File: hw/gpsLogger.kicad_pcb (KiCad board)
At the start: 4 copper layers, 41 x 72.8 mm, 210 parts, among them IC1 MSP430F55xx, P1 USB_OTG, Q2 FG6943010R, SW1 SW_PUSH, U1 MAX_M8Q, U2 MCP73812, U3 uSD, U4 MIC2091, U5 MIC2091, U6 TPS78230, X1 CRYSTAL_SMD

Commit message: Finished routing
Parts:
- removed the REF** at (150.2, 122.0)
- removed the REF** at (152.2, 122.0)
- removed the REF** at (156.2, 122.0)
- removed the REF** at (150.2, 118.0)
- removed the REF** at (150.2, 120.0)
- removed the REF** at (156.2, 120.0)
- removed the REF** at (152.2, 120.0)
- removed the REF** at (164.2, 107.6)
- removed the REF** at (150.0, 97.2)
- removed the REF** at (170.2, 108.0)
- removed the REF** at (170.2, 110.0)
- removed the REF** at (165.2, 120.0)
- removed the REF** at (170.2, 122.0)
- removed the REF** at (168.2, 122.0)
- removed the REF** at (168.2, 124.0)
- removed the REF** at (168.2, 126.0)
- removed the REF** at (164.2, 128.0)
- removed the REF** at (164.2, 130.0)
- added P2: CONN_01X02, footprints:BM02B-GHS-TBT, F.Cu at (166.4, 132.2)
- added REF**: SolderWirePad_single_0-8mmDrill, Wire_Pads:SolderWirePad_single_0-8mmDrill, F.Cu at (153.2, 115.4)
- added REF**: SolderWirePad_single_0-8mmDrill, Wire_Pads:SolderWirePad_single_0-8mmDrill, F.Cu at (169.0, 115.0)
- added REF**: SolderWirePad_single_0-8mmDrill, Wire_Pads:SolderWirePad_single_0-8mmDrill, F.Cu at (158.2, 68.0)
- added REF**: SolderWirePad_single_0-8mmDrill, Wire_Pads:SolderWirePad_single_0-8mmDrill, F.Cu at (168.8, 80.6)
- added REF**: SolderWirePad_single_0-8mmDrill, Wire_Pads:SolderWirePad_single_0-8mmDrill, F.Cu at (164.4, 99.6)
- added REF**: SolderWirePad_single_0-8mmDrill, Wire_Pads:SolderWirePad_single_0-8mmDrill, F.Cu at (162.0, 108.0)
- added REF**: SolderWirePad_single_0-8mmDrill, Wire_Pads:SolderWirePad_single_0-8mmDrill, F.Cu at (156.0, 108.0)
- added REF**: SolderWirePad_single_0-8mmDrill, Wire_Pads:SolderWirePad_single_0-8mmDrill, F.Cu at (154.0, 108.0)
- added REF**: SolderWirePad_single_0-8mmDrill, Wire_Pads:SolderWirePad_single_0-8mmDrill, F.Cu at (152.0, 108.0)
- added REF**: SolderWirePad_single_0-8mmDrill, Wire_Pads:SolderWirePad_single_0-8mmDrill, F.Cu at (168.4, 106.8)
- added REF**: SolderWirePad_single_0-8mmDrill, Wire_Pads:SolderWirePad_single_0-8mmDrill, F.Cu at (164.0, 124.0)
- added REF**: SolderWirePad_single_0-8mmDrill, Wire_Pads:SolderWirePad_single_0-8mmDrill, F.Cu at (153.4, 124.0)
- added REF**: SolderWirePad_single_0-8mmDrill, Wire_Pads:SolderWirePad_single_0-8mmDrill, F.Cu at (164.0, 122.0)
- added REF**: SolderWirePad_single_0-8mmDrill, Wire_Pads:SolderWirePad_single_0-8mmDrill, F.Cu at (164.0, 120.0)
- added REF**: SolderWirePad_single_0-8mmDrill, Wire_Pads:SolderWirePad_single_0-8mmDrill, F.Cu at (164.0, 118.0)
- added REF**: SolderWirePad_single_0-8mmDrill, Wire_Pads:SolderWirePad_single_0-8mmDrill, F.Cu at (164.0, 116.0)
- added REF**: SolderWirePad_single_0-8mmDrill, Wire_Pads:SolderWirePad_single_0-8mmDrill, F.Cu at (162.0, 116.0)
- added REF**: SolderWirePad_single_0-8mmDrill, Wire_Pads:SolderWirePad_single_0-8mmDrill, F.Cu at (162.0, 118.0)
- added REF**: SolderWirePad_single_0-8mmDrill, Wire_Pads:SolderWirePad_single_0-8mmDrill, F.Cu at (160.0, 118.0)
- added REF**: SolderWirePad_single_0-8mmDrill, Wire_Pads:SolderWirePad_single_0-8mmDrill, F.Cu at (158.0, 118.0)
- added REF**: SolderWirePad_single_0-8mmDrill, Wire_Pads:SolderWirePad_single_0-8mmDrill, F.Cu at (158.0, 122.0)
- added REF**: SolderWirePad_single_0-8mmDrill, Wire_Pads:SolderWirePad_single_0-8mmDrill, F.Cu at (158.0, 124.0)
- added REF**: SolderWirePad_single_0-8mmDrill, Wire_Pads:SolderWirePad_single_0-8mmDrill, F.Cu at (151.2, 120.4)
- added REF**: SolderWirePad_single_0-8mmDrill, Wire_Pads:SolderWirePad_single_0-8mmDrill, F.Cu at (160.0, 124.0)
- added REF**: SolderWirePad_single_0-8mmDrill, Wire_Pads:SolderWirePad_single_0-8mmDrill, F.Cu at (160.0, 122.0)
- added REF**: SolderWirePad_single_0-8mmDrill, Wire_Pads:SolderWirePad_single_0-8mmDrill, F.Cu at (150.0, 123.0)
- added REF**: SolderWirePad_single_0-8mmDrill, Wire_Pads:SolderWirePad_single_0-8mmDrill, F.Cu at (171.8, 110.0)
- added REF**: SolderWirePad_single_0-8mmDrill, Wire_Pads:SolderWirePad_single_0-8mmDrill, F.Cu at (171.2, 118.0)
- added REF**: SolderWirePad_single_0-8mmDrill, Wire_Pads:SolderWirePad_single_0-8mmDrill, F.Cu at (170.8, 120.0)
- added REF**: SolderWirePad_single_0-8mmDrill, Wire_Pads:SolderWirePad_single_0-8mmDrill, F.Cu at (170.6, 122.0)
- added REF**: SolderWirePad_single_0-8mmDrill, Wire_Pads:SolderWirePad_single_0-8mmDrill, F.Cu at (170.6, 124.0)
- ANT1, U1: moved to B.Cu
- FB1: footprint Resistors_SMD:R_0805 -> Resistors_SMD:R_0603
- moved REF** 13.1 mm to (148.0, 86.0)
- moved ANT1 11.4 mm to (149.8, 117.0), turned to 180 degrees
- moved REF** 8.85 mm to (148.0, 90.0)
- moved C5 8.63 mm to (153.3, 117.5), turned to 90 degrees
- moved U4 8.36 mm to (168.4, 109.4), turned to 270 degrees
- moved U1 8.07 mm to (160.8, 120.0), turned to 0 degrees
- moved R5 7.56 mm to (168.2, 116.8), turned to 90 degrees
- moved L2 7.52 mm to (165.8, 112.6), turned to 270 degrees
- moved R6 6.42 mm to (153.3, 120.0)
- moved R8 6.00 mm to (169.8, 116.8), turned to 270 degrees
- moved REF** 5.75 mm to (151.3, 119.0)
- moved L1 4.88 mm to (151.8, 121.5)
- moved R9 4.80 mm to (168.4, 112.4), turned to 180 degrees
- moved C13 4.53 mm to (168.4, 126.0), turned to 270 degrees
- moved REF** 3.94 mm to (148.0, 98.0)
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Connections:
- IC1 pad 19: Net-(IC1-Pad19) -> ~CHG
- IC1 pad 52: Net-(IC1-Pad52) -> /DM
- IC1 pad 65: GND -> (no net)
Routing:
- net ~CHG: track 0.00 -> 60.8 mm, vias 0 -> 4
- net GPS_BACKUP: track 23.5 -> 42.8 mm, vias 1 -> 2
- net GPS_PPS: track 24.8 -> 41.3 mm, vias 1 -> 2
- net GPS_MOSI: track 28.0 -> 41.5 mm, vias 1 -> 2
- net GPS_MISO: track 28.7 -> 40.6 mm, vias 1 -> 2
- net Net-(R5-Pad1): track 6.08 -> 14.3 mm, vias 1 -> 2
- net Net-(R8-Pad2): track 15.3 -> 9.36 mm
- net +3V3: track 25.3 -> 20.1 mm
- net GPS_VCC_RF: track 6.82 -> 2.00 mm, vias 1 -> 0
- net +BATT: track 23.1 -> 25.9 mm, vias 0 -> 1
- net GPS_VCC: track 56.9 -> 54.4 mm, vias 4 -> 3
- net GND: track 29.7 -> 31.7 mm, vias 3 -> 1
- net GPS_PWR_FAULT: track 36.1 -> 34.3 mm
- net Net-(IC1-Pad52): track 1.33 -> 0.00 mm
- net /DM: track 7.12 -> 8.45 mm
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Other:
- outline, holes or cut-outs redrawn
- board text removed: "github.com/Greeeg/gpsLogger"

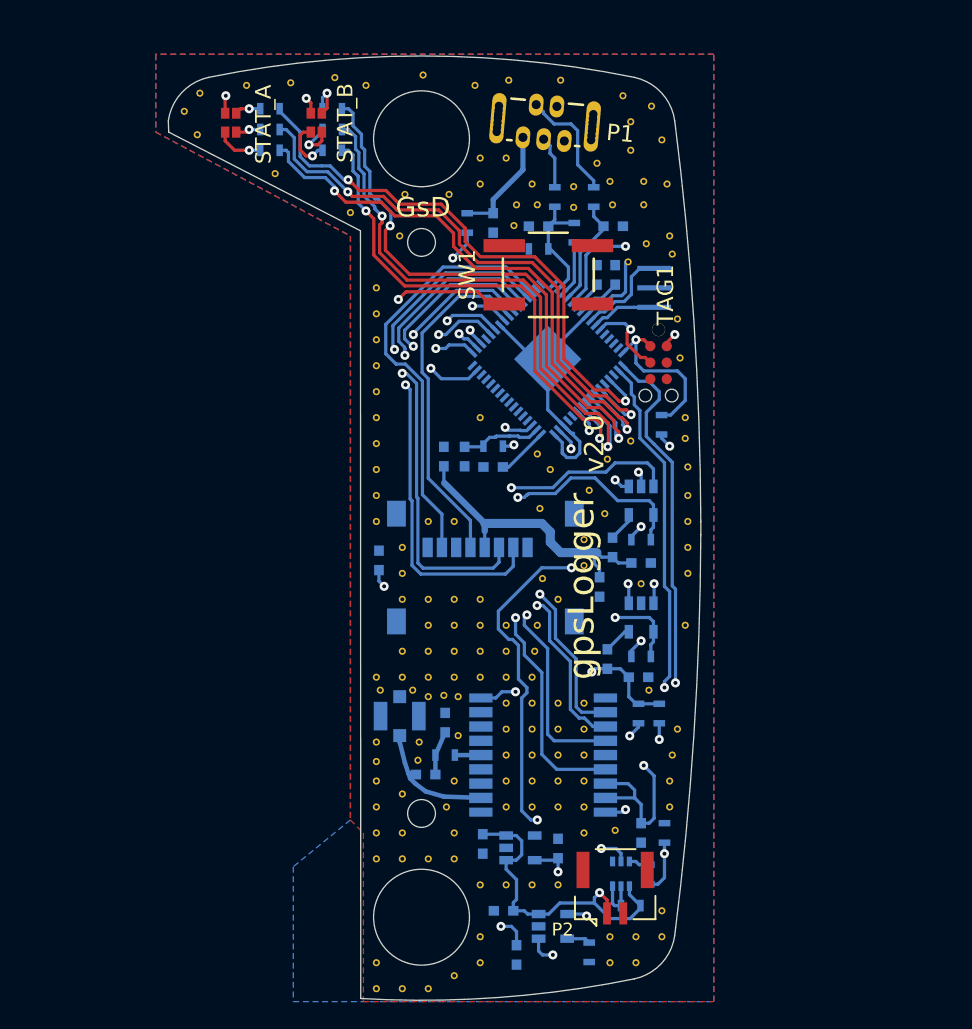
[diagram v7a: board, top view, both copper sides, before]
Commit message: Added PCB mount antenna and LNA + SAW filter. Re-routed PCB
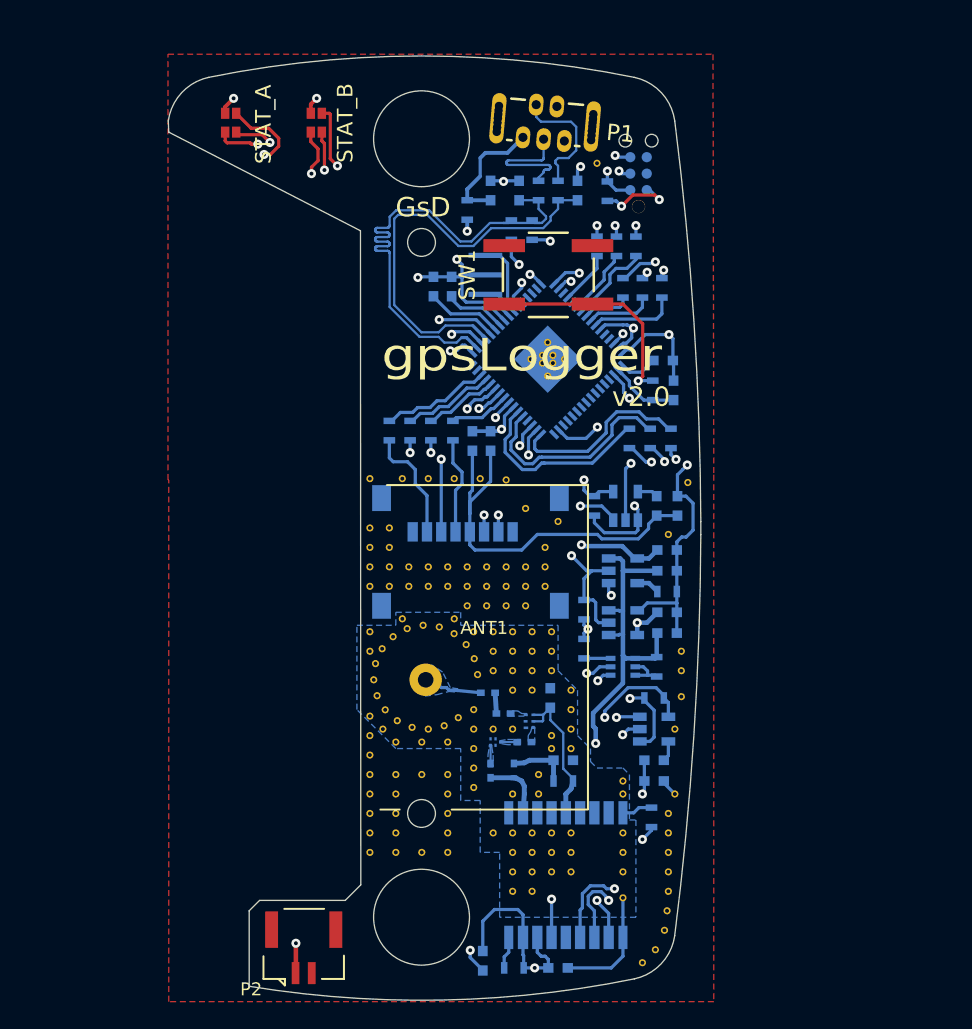
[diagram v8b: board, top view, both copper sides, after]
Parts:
- removed the REF** at (153.2, 115.4)
- removed the REF** at (169.0, 115.0)
- removed the REF** at (168.0, 136.0)
- removed the REF** at (168.0, 134.0)
- removed the REF** at (166.0, 134.0)
- removed the REF** at (162.0, 124.0)
- removed the REF** at (162.0, 122.0)
- removed the REF** at (162.0, 120.0)
- removed the REF** at (166.4, 125.8)
- removed the REF** at (164.0, 126.0)
- removed the REF** at (162.0, 130.0)
- removed the REF** at (160.0, 130.0)
- removed the REF** at (158.2, 68.0)
- removed the REF** at (158.0, 130.0)
- removed the REF** at (156.0, 130.0)
- removed the REF** at (148.0, 124.0)
- removed the REF** at (148.0, 126.0)
- removed the REF** at (150.0, 126.0)
- removed the REF** at (154.0, 126.0)
- removed the REF** at (148.0, 128.0)
- removed the REF** at (150.0, 128.0)
- removed the REF** at (154.0, 128.0)
- removed the REF** at (152.0, 128.0)
- removed the REF** at (168.8, 80.6)
- removed the REF** at (148.0, 122.0)
- removed the REF** at (154.0, 122.0)
- removed the REF** at (148.0, 114.0)
- removed the REF** at (148.0, 119.0)
- removed the REF** at (148.3, 115.0)
- removed the REF** at (148.0, 120.5)
- removed the REF** at (150.0, 112.0)
- removed the REF** at (150.0, 114.0)
- removed the REF** at (150.8, 115.0)
- removed the REF** at (160.0, 120.0)
- removed the REF** at (164.4, 99.6)
- removed the REF** at (158.0, 120.0)
- removed the REF** at (154.3, 118.5)
- removed the REF** at (160.0, 116.0)
- removed the REF** at (158.0, 116.0)
- removed the REF** at (154.3, 115.5)
- removed the REF** at (151.3, 119.0)
- removed the REF** at (152.0, 115.5)
- removed the REF** at (160.0, 114.0)
- removed the REF** at (158.0, 114.0)
- removed the REF** at (154.0, 114.0)
- removed the REF** at (162.0, 108.0)
- removed the REF** at (156.0, 114.0)
- removed the REF** at (152.0, 114.0)
- removed the REF** at (160.2, 112.0)
- removed the REF** at (158.0, 112.0)
- removed the REF** at (154.0, 112.0)
- removed the REF** at (156.0, 112.0)
- removed the REF** at (152.0, 112.0)
- removed the REF** at (158.0, 110.0)
- removed the REF** at (156.0, 110.0)
- removed the REF** at (156.0, 108.0)
- removed the REF** at (154.0, 110.0)
- removed the REF** at (152.0, 110.0)
- removed the REF** at (171.8, 95.6)
- removed the REF** at (171.8, 94.0)
- removed the REF** at (161.4, 98.0)
- removed the REF** at (160.4, 96.8)
- removed the REF** at (165.8, 97.2)
- removed the REF** at (167.6, 95.8)
- removed the REF** at (164.0, 103.4)
- removed the REF** at (164.0, 105.4)
- removed the REF** at (154.0, 108.0)
- removed the REF** at (150.0, 106.0)
- removed the REF** at (150.0, 108.0)
- removed the REF** at (150.0, 104.0)
- removed the REF** at (160.8, 106.4)
- removed the REF** at (152.0, 102.0)
- removed the REF** at (154.0, 102.0)
- removed the REF** at (152.0, 108.0)
- removed the REF** at (168.4, 106.8)
- removed the REF** at (164.0, 124.0)
- removed the REF** at (153.4, 124.0)
- removed the REF** at (164.0, 122.0)
- removed the REF** at (164.0, 120.0)
- removed the REF** at (164.0, 118.0)
- removed the REF** at (164.0, 116.0)
- removed the REF** at (162.0, 116.0)
- removed the REF** at (162.0, 118.0)
- removed the REF** at (160.0, 118.0)
- removed the REF** at (158.0, 118.0)
- removed the REF** at (158.0, 122.0)
- removed the REF** at (158.0, 124.0)
- removed the REF** at (151.2, 120.4)
- removed the REF** at (160.0, 124.0)
- removed the REF** at (160.0, 122.0)
- removed the REF** at (172.0, 97.8)
- removed the REF** at (171.4, 89.4)
- removed the REF** at (170.8, 81.4)
- removed the REF** at (171.2, 86.4)
- removed the REF** at (167.4, 82.0)
- removed the REF** at (162.2, 68.0)
- removed the REF** at (158.0, 74.0)
- removed the REF** at (156.0, 76.0)
- removed the REF** at (150.0, 123.0)
- removed the REF** at (158.6, 79.2)
- removed the REF** at (158.8, 77.6)
- removed the REF** at (160.4, 77.6)
- removed the REF** at (163.2, 77.8)
- removed the REF** at (163.2, 76.2)
- removed the REF** at (160.0, 76.0)
- removed the REF** at (167.6, 71.2)
- removed the REF** at (167.6, 73.4)
- removed the REF** at (168.6, 75.8)
- removed the REF** at (168.6, 77.6)
- removed the REF** at (171.8, 110.0)
- removed the REF** at (166.2, 77.6)
- removed the REF** at (166.0, 75.8)
- removed the REF** at (170.6, 80.0)
- removed the REF** at (170.4, 76.0)
- removed the REF** at (170.0, 72.6)
- removed the REF** at (169.2, 70.0)
- removed the REF** at (167.0, 69.2)
- removed the REF** at (140.2, 75.2)
- removed the REF** at (134.2, 72.2)
- removed the REF** at (171.2, 118.0)
- removed the REF** at (133.2, 70.4)
- removed the REF** at (134.4, 69.0)
- removed the REF** at (144.8, 67.8)
- removed the REF** at (141.4, 68.2)
- removed the REF** at (138.0, 68.4)
- removed the REF** at (147.2, 68.4)
- removed the REF** at (151.6, 67.6)
- removed the REF** at (155.6, 68.4)
- removed the REF** at (156.0, 74.0)
- removed the REF** at (153.6, 76.8)
- removed the REF** at (170.8, 120.0)
- removed the REF** at (150.2, 76.8)
- removed the REF** at (146.0, 78.2)
- removed the REF** at (149.8, 80.0)
- removed the REF** at (148.0, 84.0)
- removed the REF** at (148.0, 88.0)
- removed the REF** at (148.0, 92.0)
- removed the REF** at (148.0, 96.0)
- removed the REF** at (148.0, 100.0)
- removed the REF** at (148.0, 102.0)
- removed the REF** at (148.0, 98.0)
- removed the REF** at (170.6, 122.0)
- removed the REF** at (148.0, 94.0)
- removed the REF** at (148.0, 86.0)
- removed the REF** at (148.0, 90.0)
- removed the REF** at (156.0, 94.0)
- removed the REF** at (160.6, 101.0)
- removed the REF** at (165.6, 101.4)
- removed the REF** at (172.0, 100.0)
- removed the REF** at (172.0, 102.0)
- removed the REF** at (172.0, 104.0)
- removed the REF** at (172.0, 106.0)
- removed the REF** at (170.6, 124.0)
- removed the REF** at (154.0, 137.0)
- removed the REF** at (148.0, 136.0)
- removed the REF** at (148.0, 138.0)
- removed the REF** at (150.0, 138.0)
- removed the REF** at (152.0, 138.0)
- removed the REF** at (156.0, 136.0)
- removed the REF** at (156.0, 134.0)
- removed the REF** at (170.0, 132.0)
- removed the REF** at (170.0, 134.0)
- removed the REF** at (166.0, 136.0)
- added C19: 47pF, Capacitors_SMD:C_0402, B.Cu at (156.6, 115.2)
- added C20: 1nF, Capacitors_SMD:C_0603, B.Cu at (161.4, 115.6)
- added C21: 47pF, Capacitors_SMD:C_0402, B.Cu at (159.4, 119.0)
- added C22: 47pF, Capacitors_SMD:C_0402, B.Cu at (156.8, 121.2)
- added FLT1: B8813, footprints:SAW-5, B.Cu at (157.2, 119.0)
- added L4: 5.6nH, Capacitors_SMD:C_0402, B.Cu at (157.8, 116.8)
- added R22: 2k2, Resistors_SMD:R_0603, B.Cu at (149.0, 95.0)
- added R23: 2k2, Resistors_SMD:R_0603, B.Cu at (150.6, 95.0)
- added R24: 2k2, Resistors_SMD:R_0603, B.Cu at (152.2, 95.0)
- added R25: 2k2, Resistors_SMD:R_0603, B.Cu at (153.9, 95.0)
- added R26: 2k2, Resistors_SMD:R_0603, B.Cu at (167.5, 95.6)
- added R27: 2k2, Resistors_SMD:R_0603, B.Cu at (169.1, 95.6)
- added R28: 2k2, Resistors_SMD:R_0603, B.Cu at (170.7, 95.6)
- added REF**1: SolderWirePad_single_0-8mmDrill, Wire_Pads:SolderWirePad_single_0-8mmDrill, F.Cu at (160.8, 89.8)
- added REF**1: SolderWirePad_single_0-8mmDrill, Wire_Pads:SolderWirePad_single_0-8mmDrill, F.Cu at (155.0, 108.5)
- added REF**1: SolderWirePad_single_0-8mmDrill, Wire_Pads:SolderWirePad_single_0-8mmDrill, F.Cu at (147.5, 117.0)
- added REF**1: SolderWirePad_single_0-8mmDrill, Wire_Pads:SolderWirePad_single_0-8mmDrill, F.Cu at (148.5, 118.0)
- added REF**1: SolderWirePad_single_0-8mmDrill, Wire_Pads:SolderWirePad_single_0-8mmDrill, F.Cu at (149.5, 119.0)
- added REF**1: SolderWirePad_single_0-8mmDrill, Wire_Pads:SolderWirePad_single_0-8mmDrill, F.Cu at (151.5, 119.0)
- added REF**1: SolderWirePad_single_0-8mmDrill, Wire_Pads:SolderWirePad_single_0-8mmDrill, F.Cu at (153.5, 119.0)
- added REF**1: SolderWirePad_single_0-8mmDrill, Wire_Pads:SolderWirePad_single_0-8mmDrill, F.Cu at (155.5, 122.5)
- added REF**1: SolderWirePad_single_0-8mmDrill, Wire_Pads:SolderWirePad_single_0-8mmDrill, F.Cu at (155.5, 121.0)
- added REF**1: SolderWirePad_single_0-8mmDrill, Wire_Pads:SolderWirePad_single_0-8mmDrill, F.Cu at (155.5, 119.5)
- added REF**1: SolderWirePad_single_0-8mmDrill, Wire_Pads:SolderWirePad_single_0-8mmDrill, F.Cu at (158.5, 123.0)
- added REF**1: SolderWirePad_single_0-8mmDrill, Wire_Pads:SolderWirePad_single_0-8mmDrill, F.Cu at (160.5, 121.5)
- added REF**1: SolderWirePad_single_0-8mmDrill, Wire_Pads:SolderWirePad_single_0-8mmDrill, F.Cu at (159.5, 108.5)
- added REF**1: SolderWirePad_single_0-8mmDrill, Wire_Pads:SolderWirePad_single_0-8mmDrill, F.Cu at (160.5, 123.0)
- added REF**1: SolderWirePad_single_0-8mmDrill, Wire_Pads:SolderWirePad_single_0-8mmDrill, F.Cu at (155.5, 116.5)
- added REF**1: SolderWirePad_single_0-8mmDrill, Wire_Pads:SolderWirePad_single_0-8mmDrill, F.Cu at (155.5, 118.0)
- added REF**1: SolderWirePad_single_0-8mmDrill, Wire_Pads:SolderWirePad_single_0-8mmDrill, F.Cu at (157.0, 118.0)
- added REF**1: SolderWirePad_single_0-8mmDrill, Wire_Pads:SolderWirePad_single_0-8mmDrill, F.Cu at (158.5, 118.0)
- added REF**1: SolderWirePad_single_0-8mmDrill, Wire_Pads:SolderWirePad_single_0-8mmDrill, F.Cu at (161.5, 118.5)
- added REF**1: SolderWirePad_single_0-8mmDrill, Wire_Pads:SolderWirePad_single_0-8mmDrill, F.Cu at (161.5, 119.5)
- added REF**1: SolderWirePad_single_0-8mmDrill, Wire_Pads:SolderWirePad_single_0-8mmDrill, F.Cu at (163.0, 119.5)
- added REF**1: SolderWirePad_single_0-8mmDrill, Wire_Pads:SolderWirePad_single_0-8mmDrill, F.Cu at (163.0, 118.0)
- added REF**1: SolderWirePad_single_0-8mmDrill, Wire_Pads:SolderWirePad_single_0-8mmDrill, F.Cu at (163.0, 116.5)
- added REF**1: SolderWirePad_single_0-8mmDrill, Wire_Pads:SolderWirePad_single_0-8mmDrill, F.Cu at (158.0, 108.5)
- added REF**1: SolderWirePad_single_0-8mmDrill, Wire_Pads:SolderWirePad_single_0-8mmDrill, F.Cu at (163.0, 115.0)
- added REF**1: SolderWirePad_single_0-8mmDrill, Wire_Pads:SolderWirePad_single_0-8mmDrill, F.Cu at (160.0, 115.0)
- added REF**1: SolderWirePad_single_0-8mmDrill, Wire_Pads:SolderWirePad_single_0-8mmDrill, F.Cu at (158.5, 115.0)
- added REF**1: SolderWirePad_single_0-8mmDrill, Wire_Pads:SolderWirePad_single_0-8mmDrill, F.Cu at (157.0, 113.5)
- added REF**1: SolderWirePad_single_0-8mmDrill, Wire_Pads:SolderWirePad_single_0-8mmDrill, F.Cu at (158.5, 113.5)
- added REF**1: SolderWirePad_single_0-8mmDrill, Wire_Pads:SolderWirePad_single_0-8mmDrill, F.Cu at (160.0, 113.5)
- added REF**1: SolderWirePad_single_0-8mmDrill, Wire_Pads:SolderWirePad_single_0-8mmDrill, F.Cu at (161.5, 113.5)
- added REF**1: SolderWirePad_single_0-8mmDrill, Wire_Pads:SolderWirePad_single_0-8mmDrill, F.Cu at (161.5, 112.0)
- added REF**1: SolderWirePad_single_0-8mmDrill, Wire_Pads:SolderWirePad_single_0-8mmDrill, F.Cu at (160.0, 112.0)
- added REF**1: SolderWirePad_single_0-8mmDrill, Wire_Pads:SolderWirePad_single_0-8mmDrill, F.Cu at (158.5, 112.0)
- added REF**1: SolderWirePad_single_0-8mmDrill, Wire_Pads:SolderWirePad_single_0-8mmDrill, F.Cu at (149.0, 102.5)
- added REF**1: SolderWirePad_single_0-8mmDrill, Wire_Pads:SolderWirePad_single_0-8mmDrill, F.Cu at (157.0, 112.0)
- added REF**1: SolderWirePad_single_0-8mmDrill, Wire_Pads:SolderWirePad_single_0-8mmDrill, F.Cu at (155.5, 110.5)
- added REF**1: SolderWirePad_single_0-8mmDrill, Wire_Pads:SolderWirePad_single_0-8mmDrill, F.Cu at (157.0, 110.5)
- added REF**1: SolderWirePad_single_0-8mmDrill, Wire_Pads:SolderWirePad_single_0-8mmDrill, F.Cu at (158.5, 110.5)
- added REF**1: SolderWirePad_single_0-8mmDrill, Wire_Pads:SolderWirePad_single_0-8mmDrill, F.Cu at (160.0, 110.5)
- added REF**1: SolderWirePad_single_0-8mmDrill, Wire_Pads:SolderWirePad_single_0-8mmDrill, F.Cu at (161.5, 110.5)
- added REF**1: SolderWirePad_single_0-8mmDrill, Wire_Pads:SolderWirePad_single_0-8mmDrill, F.Cu at (158.0, 98.8)
- added REF**1: SolderWirePad_single_0-8mmDrill, Wire_Pads:SolderWirePad_single_0-8mmDrill, F.Cu at (156.0, 98.7)
- added REF**1: SolderWirePad_single_0-8mmDrill, Wire_Pads:SolderWirePad_single_0-8mmDrill, F.Cu at (154.0, 98.7)
- added REF**1: SolderWirePad_single_0-8mmDrill, Wire_Pads:SolderWirePad_single_0-8mmDrill, F.Cu at (152.0, 98.7)
- added REF**1: SolderWirePad_single_0-8mmDrill, Wire_Pads:SolderWirePad_single_0-8mmDrill, F.Cu at (147.5, 102.5)
- added REF**1: SolderWirePad_single_0-8mmDrill, Wire_Pads:SolderWirePad_single_0-8mmDrill, F.Cu at (150.0, 98.7)
- added REF**1: SolderWirePad_single_0-8mmDrill, Wire_Pads:SolderWirePad_single_0-8mmDrill, F.Cu at (147.5, 98.7)
- added REF**1: SolderWirePad_single_0-8mmDrill, Wire_Pads:SolderWirePad_single_0-8mmDrill, F.Cu at (147.5, 104.0)
- added REF**1: SolderWirePad_single_0-8mmDrill, Wire_Pads:SolderWirePad_single_0-8mmDrill, F.Cu at (149.0, 104.0)
- added REF**1: SolderWirePad_single_0-8mmDrill, Wire_Pads:SolderWirePad_single_0-8mmDrill, F.Cu at (161.0, 104.0)
- added REF**1: SolderWirePad_single_0-8mmDrill, Wire_Pads:SolderWirePad_single_0-8mmDrill, F.Cu at (147.5, 107.0)
- added REF**1: SolderWirePad_single_0-8mmDrill, Wire_Pads:SolderWirePad_single_0-8mmDrill, F.Cu at (159.5, 107.0)
- added REF**1: SolderWirePad_single_0-8mmDrill, Wire_Pads:SolderWirePad_single_0-8mmDrill, F.Cu at (161.6, 89.8)
- added REF**1: SolderWirePad_single_0-8mmDrill, Wire_Pads:SolderWirePad_single_0-8mmDrill, F.Cu at (158.0, 107.0)
- added REF**1: SolderWirePad_single_0-8mmDrill, Wire_Pads:SolderWirePad_single_0-8mmDrill, F.Cu at (156.5, 107.0)
- added REF**1: SolderWirePad_single_0-8mmDrill, Wire_Pads:SolderWirePad_single_0-8mmDrill, F.Cu at (155.0, 107.0)
- added REF**1: SolderWirePad_single_0-8mmDrill, Wire_Pads:SolderWirePad_single_0-8mmDrill, F.Cu at (153.5, 107.0)
- added REF**1: SolderWirePad_single_0-8mmDrill, Wire_Pads:SolderWirePad_single_0-8mmDrill, F.Cu at (152.0, 107.0)
- added REF**1: SolderWirePad_single_0-8mmDrill, Wire_Pads:SolderWirePad_single_0-8mmDrill, F.Cu at (150.5, 107.0)
- added REF**1: SolderWirePad_single_0-8mmDrill, Wire_Pads:SolderWirePad_single_0-8mmDrill, F.Cu at (149.0, 107.0)
- added REF**1: SolderWirePad_single_0-8mmDrill, Wire_Pads:SolderWirePad_single_0-8mmDrill, F.Cu at (161.0, 107.0)
- added REF**1: SolderWirePad_single_0-8mmDrill, Wire_Pads:SolderWirePad_single_0-8mmDrill, F.Cu at (161.0, 105.5)
- added REF**1: SolderWirePad_single_0-8mmDrill, Wire_Pads:SolderWirePad_single_0-8mmDrill, F.Cu at (159.5, 105.5)
- added REF**1: SolderWirePad_single_0-8mmDrill, Wire_Pads:SolderWirePad_single_0-8mmDrill, F.Cu at (161.6, 89.2)
- added REF**1: SolderWirePad_single_0-8mmDrill, Wire_Pads:SolderWirePad_single_0-8mmDrill, F.Cu at (158.0, 105.5)
- added REF**1: SolderWirePad_single_0-8mmDrill, Wire_Pads:SolderWirePad_single_0-8mmDrill, F.Cu at (156.5, 105.5)
- added REF**1: SolderWirePad_single_0-8mmDrill, Wire_Pads:SolderWirePad_single_0-8mmDrill, F.Cu at (155.0, 105.5)
- added REF**1: SolderWirePad_single_0-8mmDrill, Wire_Pads:SolderWirePad_single_0-8mmDrill, F.Cu at (153.5, 105.5)
- added REF**1: SolderWirePad_single_0-8mmDrill, Wire_Pads:SolderWirePad_single_0-8mmDrill, F.Cu at (152.0, 105.5)
- added REF**1: SolderWirePad_single_0-8mmDrill, Wire_Pads:SolderWirePad_single_0-8mmDrill, F.Cu at (150.5, 105.5)
- added REF**1: SolderWirePad_single_0-8mmDrill, Wire_Pads:SolderWirePad_single_0-8mmDrill, F.Cu at (149.0, 105.5)
- added REF**1: SolderWirePad_single_0-8mmDrill, Wire_Pads:SolderWirePad_single_0-8mmDrill, F.Cu at (147.5, 105.5)
- added REF**1: SolderWirePad_single_0-8mmDrill, Wire_Pads:SolderWirePad_single_0-8mmDrill, F.Cu at (149.5, 124.5)
- added REF**1: SolderWirePad_single_0-8mmDrill, Wire_Pads:SolderWirePad_single_0-8mmDrill, F.Cu at (149.5, 123.0)
- added REF**1: SolderWirePad_single_0-8mmDrill, Wire_Pads:SolderWirePad_single_0-8mmDrill, F.Cu at (160.8, 89.2)
- added REF**1: SolderWirePad_single_0-8mmDrill, Wire_Pads:SolderWirePad_single_0-8mmDrill, F.Cu at (149.5, 121.5)
- added REF**1: SolderWirePad_single_0-8mmDrill, Wire_Pads:SolderWirePad_single_0-8mmDrill, F.Cu at (151.5, 121.5)
- added REF**1: SolderWirePad_single_0-8mmDrill, Wire_Pads:SolderWirePad_single_0-8mmDrill, F.Cu at (153.5, 121.5)
- added REF**1: SolderWirePad_single_0-8mmDrill, Wire_Pads:SolderWirePad_single_0-8mmDrill, F.Cu at (153.5, 123.0)
- added REF**1: SolderWirePad_single_0-8mmDrill, Wire_Pads:SolderWirePad_single_0-8mmDrill, F.Cu at (153.5, 124.5)
- added REF**1: SolderWirePad_single_0-8mmDrill, Wire_Pads:SolderWirePad_single_0-8mmDrill, F.Cu at (153.5, 126.0)
- added REF**1: SolderWirePad_single_0-8mmDrill, Wire_Pads:SolderWirePad_single_0-8mmDrill, F.Cu at (149.5, 126.0)
- added REF**1: SolderWirePad_single_0-8mmDrill, Wire_Pads:SolderWirePad_single_0-8mmDrill, F.Cu at (147.5, 118.5)
- added REF**1: SolderWirePad_single_0-8mmDrill, Wire_Pads:SolderWirePad_single_0-8mmDrill, F.Cu at (147.5, 120.0)
- added REF**1: SolderWirePad_single_0-8mmDrill, Wire_Pads:SolderWirePad_single_0-8mmDrill, F.Cu at (147.5, 121.5)
- added REF**1: SolderWirePad_single_0-8mmDrill, Wire_Pads:SolderWirePad_single_0-8mmDrill, F.Cu at (161.2, 90.8)
- added REF**1: SolderWirePad_single_0-8mmDrill, Wire_Pads:SolderWirePad_single_0-8mmDrill, F.Cu at (147.5, 123.0)
- added REF**1: SolderWirePad_single_0-8mmDrill, Wire_Pads:SolderWirePad_single_0-8mmDrill, F.Cu at (147.5, 124.5)
- added REF**1: SolderWirePad_single_0-8mmDrill, Wire_Pads:SolderWirePad_single_0-8mmDrill, F.Cu at (147.5, 126.0)
- added REF**1: SolderWirePad_single_0-8mmDrill, Wire_Pads:SolderWirePad_single_0-8mmDrill, F.Cu at (147.5, 127.5)
- added REF**1: SolderWirePad_single_0-8mmDrill, Wire_Pads:SolderWirePad_single_0-8mmDrill, F.Cu at (149.5, 127.5)
- added REF**1: SolderWirePad_single_0-8mmDrill, Wire_Pads:SolderWirePad_single_0-8mmDrill, F.Cu at (151.5, 127.5)
- added REF**1: SolderWirePad_single_0-8mmDrill, Wire_Pads:SolderWirePad_single_0-8mmDrill, F.Cu at (153.5, 127.5)
- added REF**1: SolderWirePad_single_0-8mmDrill, Wire_Pads:SolderWirePad_single_0-8mmDrill, F.Cu at (168.5, 136.0)
- added REF**1: SolderWirePad_single_0-8mmDrill, Wire_Pads:SolderWirePad_single_0-8mmDrill, F.Cu at (169.5, 135.0)
- added REF**1: SolderWirePad_single_0-8mmDrill, Wire_Pads:SolderWirePad_single_0-8mmDrill, F.Cu at (170.2, 133.5)
- added REF**1: SolderWirePad_single_0-8mmDrill, Wire_Pads:SolderWirePad_single_0-8mmDrill, F.Cu at (161.2, 88.2)
- added REF**1: SolderWirePad_single_0-8mmDrill, Wire_Pads:SolderWirePad_single_0-8mmDrill, F.Cu at (170.4, 132.0)
- added REF**1: SolderWirePad_single_0-8mmDrill, Wire_Pads:SolderWirePad_single_0-8mmDrill, F.Cu at (170.5, 130.5)
- added REF**1: SolderWirePad_single_0-8mmDrill, Wire_Pads:SolderWirePad_single_0-8mmDrill, F.Cu at (170.5, 129.0)
- added REF**1: SolderWirePad_single_0-8mmDrill, Wire_Pads:SolderWirePad_single_0-8mmDrill, F.Cu at (170.5, 127.5)
- added REF**1: SolderWirePad_single_0-8mmDrill, Wire_Pads:SolderWirePad_single_0-8mmDrill, F.Cu at (170.5, 126.0)
- added REF**1: SolderWirePad_single_0-8mmDrill, Wire_Pads:SolderWirePad_single_0-8mmDrill, F.Cu at (170.5, 124.5)
- added REF**1: SolderWirePad_single_0-8mmDrill, Wire_Pads:SolderWirePad_single_0-8mmDrill, F.Cu at (171.0, 123.0)
- added REF**1: SolderWirePad_single_0-8mmDrill, Wire_Pads:SolderWirePad_single_0-8mmDrill, F.Cu at (171.0, 118.0)
- added REF**1: SolderWirePad_single_0-8mmDrill, Wire_Pads:SolderWirePad_single_0-8mmDrill, F.Cu at (171.5, 115.5)
- added REF**1: SolderWirePad_single_0-8mmDrill, Wire_Pads:SolderWirePad_single_0-8mmDrill, F.Cu at (171.5, 113.5)
- added REF**1: SolderWirePad_single_0-8mmDrill, Wire_Pads:SolderWirePad_single_0-8mmDrill, F.Cu at (162.5, 89.5)
- added REF**1: SolderWirePad_single_0-8mmDrill, Wire_Pads:SolderWirePad_single_0-8mmDrill, F.Cu at (171.5, 112.0)
- added REF**1: SolderWirePad_single_0-8mmDrill, Wire_Pads:SolderWirePad_single_0-8mmDrill, F.Cu at (172.0, 99.0)
- added REF**1: SolderWirePad_single_0-8mmDrill, Wire_Pads:SolderWirePad_single_0-8mmDrill, F.Cu at (170.5, 103.0)
- added REF**1: SolderWirePad_single_0-8mmDrill, Wire_Pads:SolderWirePad_single_0-8mmDrill, F.Cu at (159.5, 101.0)
- added REF**1: SolderWirePad_single_0-8mmDrill, Wire_Pads:SolderWirePad_single_0-8mmDrill, F.Cu at (162.0, 102.0)
- added REF**1: SolderWirePad_single_0-8mmDrill, Wire_Pads:SolderWirePad_single_0-8mmDrill, F.Cu at (158.5, 130.5)
- added REF**1: SolderWirePad_single_0-8mmDrill, Wire_Pads:SolderWirePad_single_0-8mmDrill, F.Cu at (160.0, 130.5)
- added REF**1: SolderWirePad_single_0-8mmDrill, Wire_Pads:SolderWirePad_single_0-8mmDrill, F.Cu at (158.5, 129.0)
- added REF**1: SolderWirePad_single_0-8mmDrill, Wire_Pads:SolderWirePad_single_0-8mmDrill, F.Cu at (167.0, 129.0)
- added REF**1: SolderWirePad_single_0-8mmDrill, Wire_Pads:SolderWirePad_single_0-8mmDrill, F.Cu at (160.0, 129.0)
- added REF**1: SolderWirePad_single_0-8mmDrill, Wire_Pads:SolderWirePad_single_0-8mmDrill, F.Cu at (159.9, 89.5)
- added REF**1: SolderWirePad_single_0-8mmDrill, Wire_Pads:SolderWirePad_single_0-8mmDrill, F.Cu at (163.0, 129.0)
- added REF**1: SolderWirePad_single_0-8mmDrill, Wire_Pads:SolderWirePad_single_0-8mmDrill, F.Cu at (161.5, 129.0)
- added REF**1: SolderWirePad_single_0-8mmDrill, Wire_Pads:SolderWirePad_single_0-8mmDrill, F.Cu at (157.0, 126.0)
- added REF**1: SolderWirePad_single_0-8mmDrill, Wire_Pads:SolderWirePad_single_0-8mmDrill, F.Cu at (158.5, 127.5)
- added REF**1: SolderWirePad_single_0-8mmDrill, Wire_Pads:SolderWirePad_single_0-8mmDrill, F.Cu at (158.5, 126.0)
- added REF**1: SolderWirePad_single_0-8mmDrill, Wire_Pads:SolderWirePad_single_0-8mmDrill, F.Cu at (160.0, 127.5)
- added REF**1: SolderWirePad_single_0-8mmDrill, Wire_Pads:SolderWirePad_single_0-8mmDrill, F.Cu at (160.0, 126.0)
- added REF**1: SolderWirePad_single_0-8mmDrill, Wire_Pads:SolderWirePad_single_0-8mmDrill, F.Cu at (161.5, 127.5)
- added REF**1: SolderWirePad_single_0-8mmDrill, Wire_Pads:SolderWirePad_single_0-8mmDrill, F.Cu at (161.5, 126.0)
- added REF**1: SolderWirePad_single_0-8mmDrill, Wire_Pads:SolderWirePad_single_0-8mmDrill, F.Cu at (163.0, 127.5)
- added REF**1: SolderWirePad_single_0-8mmDrill, Wire_Pads:SolderWirePad_single_0-8mmDrill, F.Cu at (156.5, 108.5)
- added REF**1: SolderWirePad_single_0-8mmDrill, Wire_Pads:SolderWirePad_single_0-8mmDrill, F.Cu at (163.0, 126.0)
- added REF**1: SolderWirePad_single_0-8mmDrill, Wire_Pads:SolderWirePad_single_0-8mmDrill, F.Cu at (167.0, 131.0)
- added REF**1: SolderWirePad_single_0-8mmDrill, Wire_Pads:SolderWirePad_single_0-8mmDrill, F.Cu at (167.0, 127.5)
- added REF**1: SolderWirePad_single_0-8mmDrill, Wire_Pads:SolderWirePad_single_0-8mmDrill, F.Cu at (167.0, 126.0)
- added REF**1: SolderWirePad_single_0-8mmDrill, Wire_Pads:SolderWirePad_single_0-8mmDrill, F.Cu at (167.0, 123.0)
- added REF**1: SolderWirePad_single_0-8mmDrill, Wire_Pads:SolderWirePad_single_0-8mmDrill, F.Cu at (167.0, 122.0)
- added REF**1: SolderWirePad_single_0-8mmDrill, Wire_Pads:SolderWirePad_single_0-8mmDrill, F.Cu at (154.0, 109.5)
- added REF**1: SolderWirePad_single_0-8mmDrill, Wire_Pads:SolderWirePad_single_0-8mmDrill, F.Cu at (150.0, 109.5)
- added REF**1: SolderWirePad_single_0-8mmDrill, Wire_Pads:SolderWirePad_single_0-8mmDrill, F.Cu at (147.5, 112.0)
- added REF**1: SolderWirePad_single_0-8mmDrill, Wire_Pads:SolderWirePad_single_0-8mmDrill, F.Cu at (147.5, 110.5)
- added REF**11: SolderWirePad_single_0-8mmDrill, Wire_Pads:SolderWirePad_single_0-8mmDrill, F.Cu at (155.8, 113.8)
- added REF**12: SolderWirePad_single_0-8mmDrill, Wire_Pads:SolderWirePad_single_0-8mmDrill, F.Cu at (155.5, 112.6)
- added REF**13: SolderWirePad_single_0-8mmDrill, Wire_Pads:SolderWirePad_single_0-8mmDrill, F.Cu at (154.9, 111.5)
- added REF**14: SolderWirePad_single_0-8mmDrill, Wire_Pads:SolderWirePad_single_0-8mmDrill, F.Cu at (154.0, 110.6)
- added REF**15: SolderWirePad_single_0-8mmDrill, Wire_Pads:SolderWirePad_single_0-8mmDrill, F.Cu at (152.8, 110.1)
- added REF**16: SolderWirePad_single_0-8mmDrill, Wire_Pads:SolderWirePad_single_0-8mmDrill, F.Cu at (151.6, 110.0)
- added REF**17: SolderWirePad_single_0-8mmDrill, Wire_Pads:SolderWirePad_single_0-8mmDrill, F.Cu at (150.4, 110.3)
- added REF**18: SolderWirePad_single_0-8mmDrill, Wire_Pads:SolderWirePad_single_0-8mmDrill, F.Cu at (149.3, 110.9)
- added REF**19: SolderWirePad_single_0-8mmDrill, Wire_Pads:SolderWirePad_single_0-8mmDrill, F.Cu at (148.4, 111.8)
- added REF**2: SolderWirePad_single_0-8mmDrill, Wire_Pads:SolderWirePad_single_0-8mmDrill, F.Cu at (148.1, 115.4)
- added REF**20: SolderWirePad_single_0-8mmDrill, Wire_Pads:SolderWirePad_single_0-8mmDrill, F.Cu at (147.9, 113.0)
- added REF**3: SolderWirePad_single_0-8mmDrill, Wire_Pads:SolderWirePad_single_0-8mmDrill, F.Cu at (148.7, 116.5)
- added REF**4: SolderWirePad_single_0-8mmDrill, Wire_Pads:SolderWirePad_single_0-8mmDrill, F.Cu at (149.6, 117.4)
- added REF**5: SolderWirePad_single_0-8mmDrill, Wire_Pads:SolderWirePad_single_0-8mmDrill, F.Cu at (150.8, 117.9)
- added REF**6: SolderWirePad_single_0-8mmDrill, Wire_Pads:SolderWirePad_single_0-8mmDrill, F.Cu at (152.0, 118.0)
- added REF**7: SolderWirePad_single_0-8mmDrill, Wire_Pads:SolderWirePad_single_0-8mmDrill, F.Cu at (153.2, 117.7)
- added REF**8: SolderWirePad_single_0-8mmDrill, Wire_Pads:SolderWirePad_single_0-8mmDrill, F.Cu at (154.3, 117.1)
- added U7: BGU7007, footprints:XSON6, B.Cu at (159.8, 117.4)
- ANT1: footprint footprints:MCRF -> footprints:GPS_ANT; moved to F.Cu
- L1: footprint Capacitors_SMD:C_0603 -> Capacitors_SMD:C_0402
- TAG1: moved to B.Cu
- moved C12 34.3 mm to (162.0, 136.4), turned to 0 degrees
- moved C6 33.3 mm to (170.4, 104.2), turned to 0 degrees
- moved R18 29.2 mm to (168.0, 80.8), turned to 270 degrees
- moved C9 29.1 mm to (170.4, 105.8), turned to 0 degrees
- moved R7 28.4 mm to (170.4, 107.4), turned to 180 degrees
- moved R17 28.2 mm to (166.5, 80.8), turned to 270 degrees
- moved U2 27.9 mm to (167.0, 105.8)
- moved R21 27.5 mm to (170.0, 84.0), turned to 270 degrees
- moved R16 27.3 mm to (165.0, 80.8), turned to 270 degrees
- moved R20 26.8 mm to (168.5, 84.0), turned to 270 degrees
- moved R19 26.3 mm to (167.0, 84.0), turned to 270 degrees
- moved C10 24.9 mm to (156.2, 135.8), turned to 270 degrees
- moved P2 24.4 mm to (142.4, 136.8)
- moved R8 22.6 mm to (158.6, 136.4), turned to 180 degrees
- moved C14 21.6 mm to (170.4, 110.6), turned to 0 degrees
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- renumbered REF** to REF**1
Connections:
- net /D+ renamed /USB_IN_P
- net /D- renamed /USB_IN_N
- net /DM renamed /USB_DATA_N
- net /DP renamed /USB_DATA_P
- ANT1 pad 1: GPS_RF_IN -> /ANT_RF
- IC1 pad 33: GPS_PPS -> Net-(IC1-Pad33)
- IC1 pad 37: GPS_MOSI -> Net-(IC1-Pad37)
- IC1 pad 38: GPS_MISO -> Net-(IC1-Pad38)
- IC1 pad 41: MMC_CLK -> Net-(IC1-Pad41)
- IC1 pad 44: MMC_CS -> Net-(IC1-Pad44)
- IC1 pad 45: MMC_MOSI -> Net-(IC1-Pad45)
- IC1 pad 46: MMC_MISO -> Net-(IC1-Pad46)
- IC1 pad 65: (no net) -> GND
- P2 pad : (no net) -> GND
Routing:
- net +3V3: track 20.1 -> 135.3 mm, vias 12 -> 9
- net GND: track 31.7 -> 89.6 mm, vias 1 -> 17
- net VBUS: track 97.2 -> 44.1 mm, vias 4 -> 3
- net /LED_B_R: track 44.9 -> 3.71 mm, vias 2 -> 0
- net ~CHG: track 60.8 -> 19.8 mm, vias 4 -> 2
- net +BATT: track 25.9 -> 65.7 mm, vias 1 -> 2
- net /LED_A_R: track 43.4 -> 4.14 mm, vias 2 -> 0
- net /LED_A_G: track 44.3 -> 5.17 mm, vias 2 -> 0
- net /LED_B_G: track 43.5 -> 5.15 mm, vias 2 -> 0
- net /LED_A_B: track 44.2 -> 6.50 mm, vias 2 -> 0
- net Net-(D1-Pad4): track 3.68 -> 37.2 mm, vias 1 -> 2
- net Net-(D1-Pad2): track 1.99 -> 35.1 mm, vias 1 -> 2
- net /LED_B_B: track 39.7 -> 6.74 mm, vias 2 -> 0
- net Net-(D2-Pad2): track 3.06 -> 35.7 mm, vias 1 -> 2
- net Net-(D1-Pad3): track 1.93 -> 33.3 mm, vias 1 -> 2
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- added copper zone on B.Cu, net /ANT_RF
- added copper zone on B.Cu, net Net-(C21-Pad1)
- added copper zone on B.Cu, net Net-(C21-Pad2)
- added copper zone on B.Cu, net Net-(C22-Pad2)
- added copper zone on B.Cu, net Net-(L4-Pad2)
- removed copper zone on In1.Cu, net +3V3
- removed copper zone on In1.Cu, net GND
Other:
- outline, holes or cut-outs redrawn
- net class Power: clearance 0.2 -> 0.22
- net class USB added: clearance 0.177, trace_width 0.177, via_dia 0.7, via_drill 0.3
- rule trace_min: 0.18 -> 0.15
